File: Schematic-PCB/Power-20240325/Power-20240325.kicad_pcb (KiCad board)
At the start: 0 parts

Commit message: キッカー・MD・ラインセンサ・電源基板を更新
キッカー :
・基板外形変更後のPCBの修正が途中で止まっていたため、残りの部分を編集した

ラインセンサ :
・以前のラインセンサ回路を、コンパレータを使用する回路へと置換した
・ラベル line_threshold を、PWM出力可能な5番ピンに設定した

MD :
・キッカーもMD基板を経由させるように変更した
・ラインセンサ用にレベル変換回路を作成した

電源基板 :
・フットプリントを一部指定した
・基板外形をインポートした
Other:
- board outline added: 43.9 x 82.2 mm
- copper layers 0 -> 2

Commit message: MD基板の仮完成
DRをお願いします
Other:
- board size 43.9 x 82.2 mm -> 43.9 x 82.9 mm

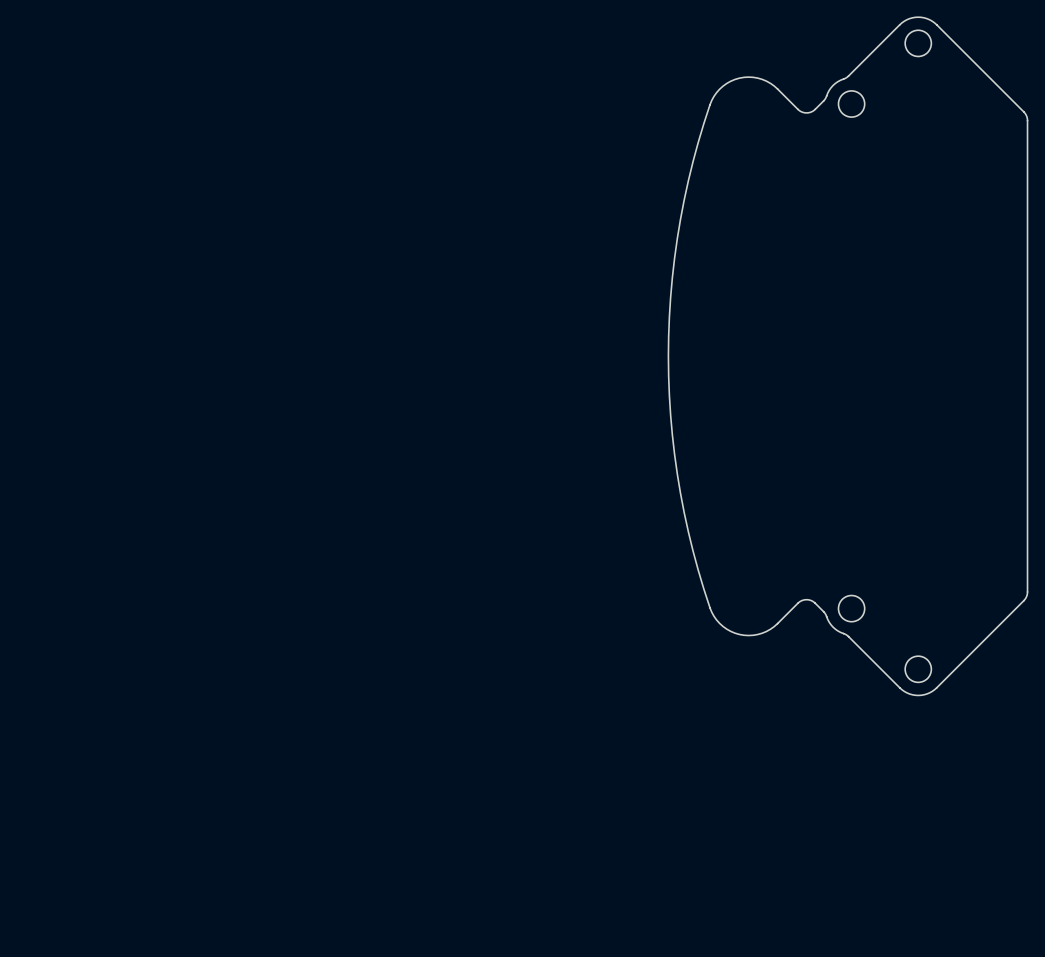
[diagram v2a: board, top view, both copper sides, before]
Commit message: 電源基板PCBの途中まで
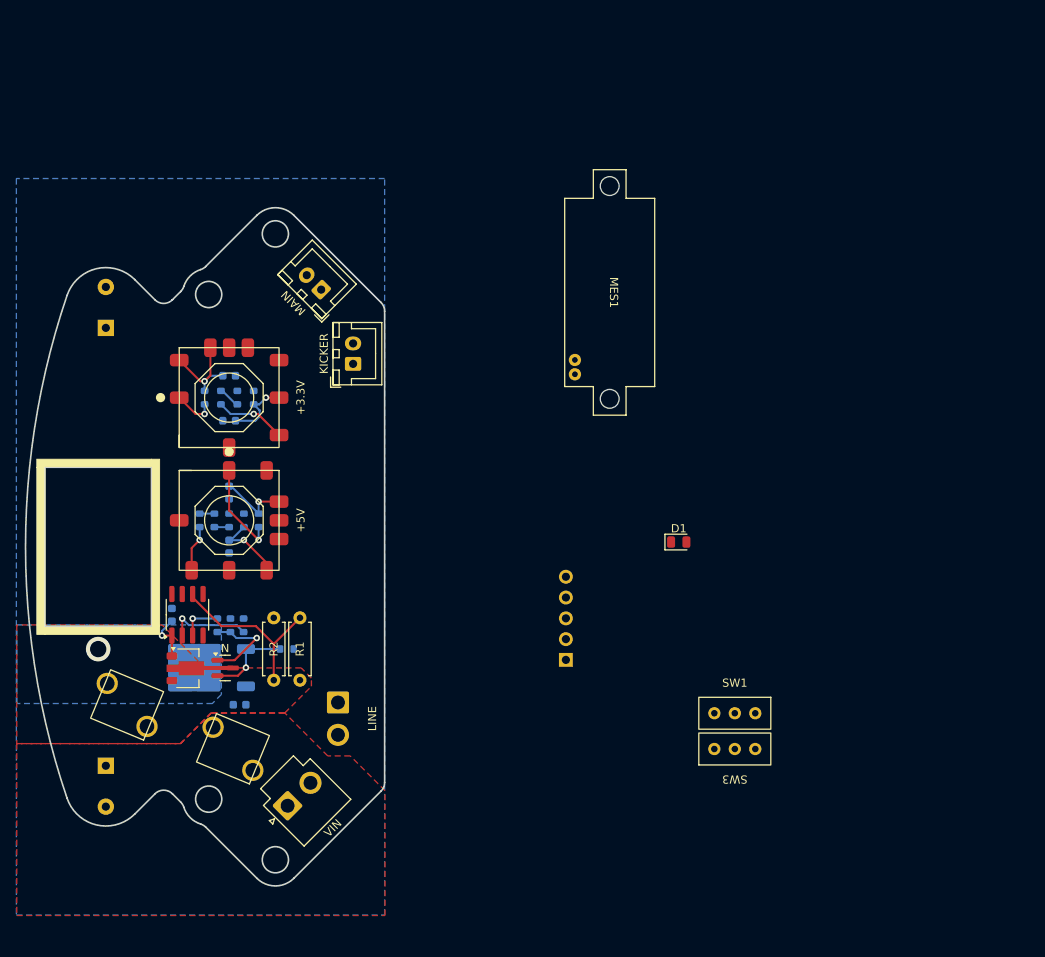
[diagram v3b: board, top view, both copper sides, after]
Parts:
- added +3.3V: ~, @2024-Power:OKL-T6-W12N-C, F.Cu at (56.0, 116.7)
- added +5V: ~, @2024-Power:OKL-T6-W12N-C, F.Cu at (56.0, 131.7)
- added 1.2K: 1.2K, Resistor_SMD:R_0603_1608Metric, B.Cu at (57.8, 131.7)
- added 1.5K: 1.5K, Resistor_SMD:R_0603_1608Metric, B.Cu at (55.0, 116.7)
- added 1.5K: 1.2K, Resistor_SMD:R_0603_1608Metric, B.Cu at (59.0, 116.7)
- added 10: 10, Resistor_SMD:R_0603_1608Metric, B.Cu at (56.0, 131.7)
- added 100: 100, Resistor_SMD:R_0603_1608Metric, B.Cu at (54.6, 144.6)
- added 10K: 10K, Resistor_SMD:R_0603_1608Metric, B.Cu at (56.2, 144.6)
- added 10u: 22uF, Capacitor_SMD:C_0603_1608Metric, B.Cu at (56.0, 119.5)
- added 10u: 10uF, Capacitor_SMD:C_0603_1608Metric, B.Cu at (56.0, 134.9)
- added 1K: 1K, Resistor_SMD:R_0603_1608Metric, B.Cu at (52.4, 131.7)
- added 1u: 1.0uF, Capacitor_SMD:C_0603_1608Metric, B.Cu at (57.3, 154.3)
- added 2.2u: 2.2uF, Capacitor_SMD:C_0603_1608Metric, B.Cu at (49.0, 143.3)
- added 20K: 20K, Resistor_SMD:R_0603_1608Metric, B.Cu at (59.6, 131.7)
- added 20K: 20K, Resistor_SMD:R_0603_1608Metric, B.Cu at (53.0, 116.7)
- added 22u: 22uF, Capacitor_SMD:C_0603_1608Metric, B.Cu at (56.0, 128.3)
- added 22u: 22uF, Capacitor_SMD:C_0603_1608Metric, B.Cu at (56.0, 114.0)
- added 330: 330, Resistor_SMD:R_0603_1608Metric, B.Cu at (57.8, 144.6)
- added 330: 330, Resistor_SMD:R_0603_1608Metric, B.Cu at (54.2, 131.7)
- added 680: 680, Resistor_SMD:R_0603_1608Metric, B.Cu at (57.0, 116.7)
- added C6: 1000uF, Capacitor_THT:CP_Radial_D10.0mm_P5.00mm, B.Cu at (40.9, 108.2)
- added C7: 1000uF, Capacitor_THT:CP_Radial_D10.0mm_P5.00mm, B.Cu at (40.9, 161.7)
- added D1: LED, LED_SMD:LED_0805_2012Metric, F.Cu at (110.9, 134.4)
- added F1: 10A/15A, @2024-Power:Fuse, F.Cu at (50.0, 157.0)
- added J2: Conn_01x05_Pin, Connector_PinSocket_2.54mm:PinSocket_1x05_P2.54mm_Vertical, B.Cu at (97.2, 148.8)
- added KICKER: Conn_01x02_Pin, Connector_JST:JST_XH_B2B-XH-A_1x02_P2.50mm_Vertical, F.Cu at (71.1, 112.6)
- added LINE: Conn_01x02_Pin, Connector_JST:JST_VH_S2P-VH_1x02_P3.96mm_Horizontal, B.Cu at (69.3, 154.0)
- added MAIN: Conn_01x02_Pin, Connector_JST:JST_XH_B2B-XH-A_1x02_P2.50mm_Vertical, F.Cu at (67.2, 103.5)
- added MES1: Voltmeter_DC, @2024-Power:VoltMeter, F.Cu at (102.5, 103.9)
- added N: NMOS, Package_TO_SOT_SMD:SOT-23, F.Cu at (55.5, 149.8)
- added P: PMOS, Package_TO_SOT_SMD:TO-252-2, B.Cu at (53.0, 149.7)
- added R1: R, Resistor_THT:R_Axial_DIN0207_L6.3mm_D2.5mm_P7.62mm_Horizontal, F.Cu at (64.7, 151.3)
- added R2: R, Resistor_THT:R_Axial_DIN0207_L6.3mm_D2.5mm_P7.62mm_Horizontal, F.Cu at (61.5, 151.3)
- added R4: 10K, Resistor_SMD:R_0603_1608Metric, B.Cu at (63.1, 147.4)
- added SW1: SW_SPDT, @2024-Power:SS12D01G4, F.Cu at (117.8, 155.3)
- added SW2: Locker-SW, @2024-Power:RA1113112R, F.Cu at (40.0, 135.0)
- added SW3: SW_SPDT, @2024-Power:SS12D01G4, F.Cu at (117.8, 159.7)
- added U1: PIC12F683-IMC, Package_SO:SOP-8_3.76x4.96mm_P1.27mm, F.Cu at (50.9, 143.3)
- added U3: ~, Package_TO_SOT_SMD:SOT-89-3, F.Cu at (51.0, 149.8)
- added VIN: Conn_01x02_Pin, Connector_JST:JST_VH_B2P-VH-B_1x02_P3.96mm_Vertical, F.Cu at (63.1, 166.6)
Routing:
- net ICSPCLK: track 0.00 -> 21.6 mm
- net VIN: track 0.00 -> 21.2 mm, vias 0 -> 2
- net Net-(SW3-A): track 0.00 -> 11.6 mm, vias 0 -> 1
- net Net-(Q2-G): track 0.00 -> 11.0 mm, vias 0 -> 1
- net Net-(Q1-G): track 0.00 -> 10.3 mm, vias 0 -> 1
- net Net-(U1-GP5): track 0.00 -> 10.3 mm, vias 0 -> 1
- net +5V: track 0.00 -> 9.12 mm, vias 0 -> 1
- net Net-(U2-Trim): track 0.00 -> 8.66 mm, vias 0 -> 1
- net +3.3V: track 0.00 -> 8.38 mm, vias 0 -> 1
- net GND: track 0.00 -> 7.38 mm
- net +3.3VA: track 0.00 -> 5.96 mm, vias 0 -> 1
- net Net-(U4-Trim): track 0.00 -> 5.68 mm, vias 0 -> 1
- net Net-(SW1-A): track 0.00 -> 5.10 mm, vias 0 -> 1
- net V_Control: track 0.00 -> 5.10 mm, vias 0 -> 1
- net Net-(R6-Pad2): track 0.00 -> 2.68 mm
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- added copper zone on B.Cu, net GND
- added copper zone on F.Cu, net Net-(J1-Pin_1)
- added copper zone on B.Cu, net Net-(Q1-D)
- added copper zone on F.Cu, net V_RAW
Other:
- outline, holes or cut-outs redrawn

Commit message: 電源基板PCB仮完成
DRをお願いします。
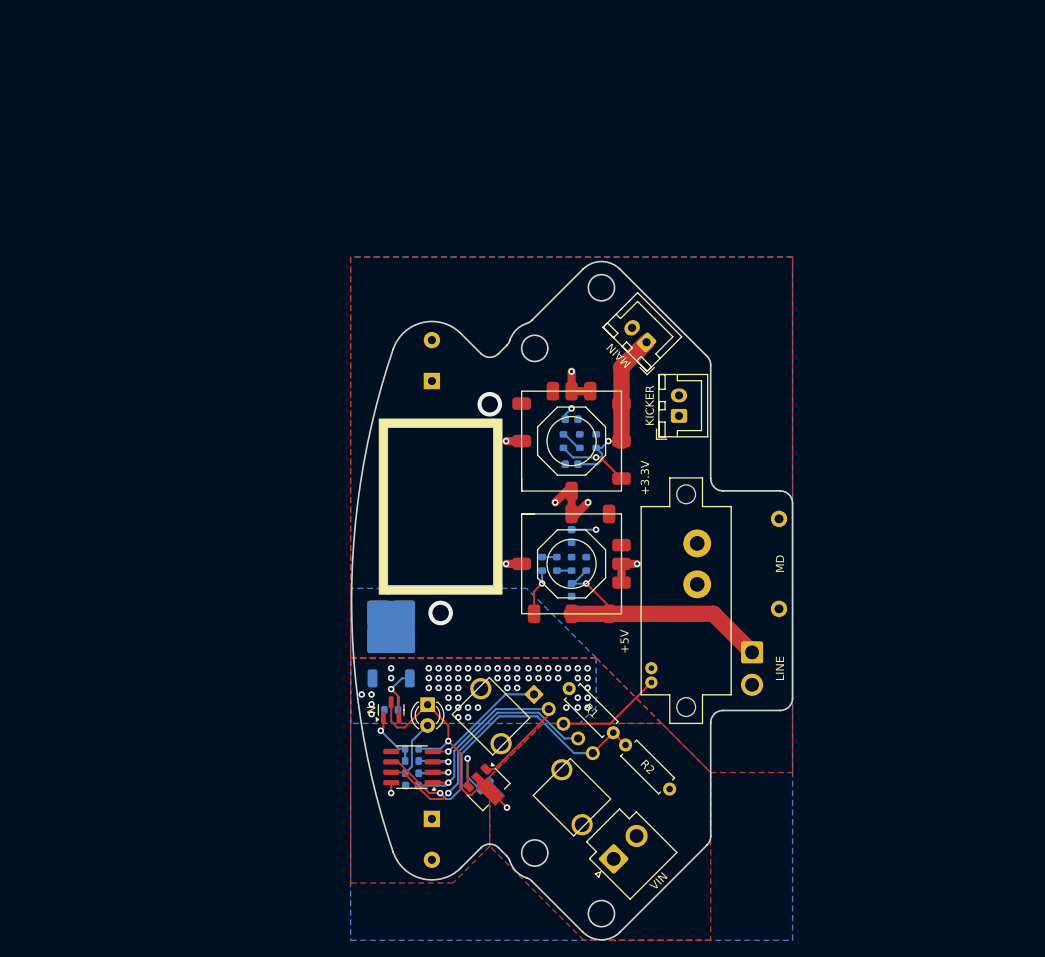
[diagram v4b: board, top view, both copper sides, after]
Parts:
- removed 20K (x2): 20K, Resistor_SMD:R_0603_1608Metric
- removed SW1, SW3: SW_SPDT, @2024-Power:SS12D01G4
- added MD: Conn_01x02_Pin, @2024-Power:XT30PW-M, B.Cu at (113.2, 137.0)
- D1: footprint LED_SMD:LED_0805_2012Metric -> LED_THT:LED_D3.0mm
- moved LINE 51.0 mm to (119.9, 147.9)
- moved R2 43.7 mm to (104.4, 159.2), turned to -45 degrees
- moved F1 43.1 mm to (92.9, 160.6), turned to 135 degrees
- moved 1K 42.2 mm to (94.2, 137.0)
- moved +3.3V 42.2 mm to (97.8, 122.0)
- moved +5V 42.2 mm to (97.8, 137.0)
- moved 1.2K 42.2 mm to (99.6, 137.0)
- moved 1.5K 42.2 mm to (96.8, 122.0)
- moved 1.5K 42.2 mm to (100.8, 122.0)
- moved 10 42.2 mm to (97.8, 137.0)
- moved 10u 42.2 mm to (97.8, 124.9)
- moved 10u 42.2 mm to (97.8, 140.2)
- moved 22u 42.2 mm to (97.8, 133.6)
- moved 22u 42.2 mm to (97.8, 119.4)
- moved 330 42.2 mm to (96.0, 137.0)
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- renumbered R4 to 10K
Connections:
- +3.3V pad 1: Net-(SW1-A) -> GND
- +5V pad 1: Net-(SW3-A) -> GND
- C7 pad 1: VIN -> V_RAW
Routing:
- net GND: track 7.38 -> 67.9 mm, vias 0 -> 9
- net ICSPDAT: track 0.00 -> 32.1 mm, vias 0 -> 1
- net +3.3VA: track 5.96 -> 34.7 mm
- net +5V: track 9.12 -> 33.1 mm
- net ICSPCLK: track 21.6 -> 40.7 mm, vias 0 -> 1
- net VIN: track 21.2 -> 5.90 mm, vias 2 -> 3
- net MCLR/VPP: track 0.00 -> 15.3 mm, vias 0 -> 1
- net +3.3V: track 8.38 -> 21.7 mm
- net Net-(SW3-A): track 11.6 -> 0.00 mm, vias 1 -> 0
- net V_RAW: track 0.00 -> 8.00 mm, vias 0 -> 58
- net Net-(D1-A): track 0.00 -> 7.61 mm
- net Net-(SW1-A): track 5.10 -> 0.00 mm, vias 1 -> 0
- net Net-(U1-GP5): track 10.3 -> 5.57 mm
- net Net-(Q2-G): track 11.0 -> 7.13 mm
- net Net-(Q1-G): track 10.3 -> 9.58 mm
- added copper zone on F.Cu, net VIN
- added copper zone on B.Cu, net V_RAW
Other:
- board size 43.9 x 82.9 mm -> 53.9 x 82.9 mm
